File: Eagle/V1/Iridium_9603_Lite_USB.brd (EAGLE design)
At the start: 34.7 x 44.2 mm, 26 parts, among them J1 SS4-10-3.50-X-D, J2 uFL, U1 SPX3819M5-L-3-3, U2 LTC3225EDDB-TRMPBFDFN300X200-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, U3 CY7C65213

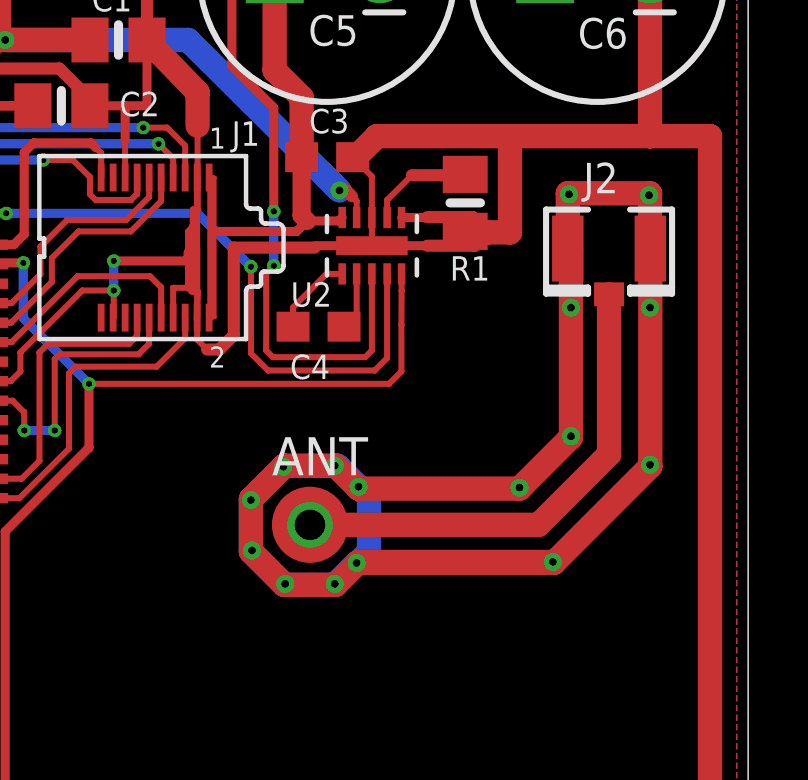
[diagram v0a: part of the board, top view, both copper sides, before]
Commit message: Updated ANT and GNDA to provide impedance of 50 Ohms
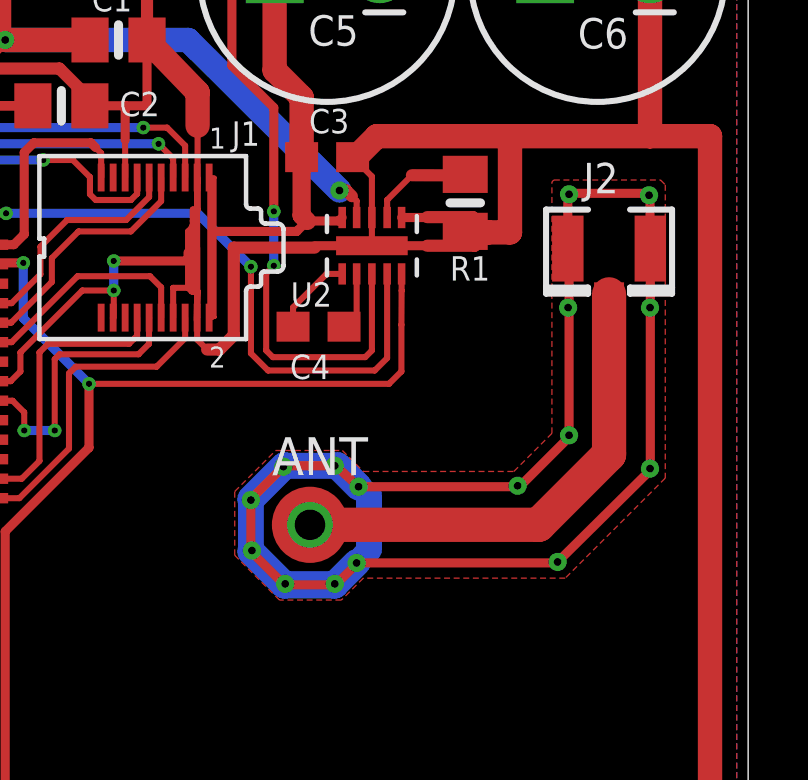
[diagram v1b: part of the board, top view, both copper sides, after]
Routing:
- net GNDA: track 69.2 -> 62.6 mm
- added copper zone on layer 1, net GNDA
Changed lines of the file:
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@@
 <wire x1="20.22475" y1="30.00375" x2="20.22475" y2="29.94025" width="0.127" layer="1"/>
 <wire x1="20.22475" y1="29.94025" x2="17.526" y2="29.94025" width="0.4064" layer="1"/>
-<polygon width="0.4064" layer="1" spacing="0.8128" pour="hatch" isolate="0.6096">
+<polygon width="0.4064" layer="1" spacing="0.8128" pour="hatch" isolate="0.6096" rank="2">
 <vertex x="0.381" y="0.381"/>
 <vertex x="0.381" y="43.815"/>
@@
 <contactref element="ANT" pad="TP"/>
 <contactref element="J2" pad="3"/>
-<wire x1="30.0355" y1="28.3835" x2="30.0355" y2="23.0505" width="0.8128" layer="1"/>
-<wire x1="30.0355" y1="23.0505" x2="27.686" y2="20.701" width="0.8128" layer="1"/>
-<wire x1="27.686" y1="20.701" x2="20.066" y2="20.701" width="0.8128" layer="1"/>
+<wire x1="30.0355" y1="28.3835" x2="30.0355" y2="23.0505" width="1.143" layer="1"/>
+<wire x1="30.0355" y1="23.0505" x2="27.686" y2="20.701" width="1.143" layer="1"/>
+<wire x1="27.686" y1="20.701" x2="20.066" y2="20.701" width="1.143" layer="1"/>
 <via x="20.066" y="20.701" extent="1-16" drill="1.016" diameter="1.397"/>
 </signal>
@@
 <contactref element="J2" pad="2"/>
 <contactref element="J2" pad="1"/>
-<wire x1="28.6605" y1="29.9085" x2="28.7655" y2="29.9085" width="0.8128" layer="1"/>
-<wire x1="28.7655" y1="29.9085" x2="28.7655" y2="23.622" width="0.8128" layer="1"/>
-<wire x1="28.7655" y1="23.622" x2="27.051" y2="21.9075" width="0.8128" layer="1"/>
-<wire x1="27.051" y1="21.9075" x2="21.68525" y2="21.9075" width="0.8128" layer="1"/>
-<wire x1="21.68525" y1="21.9075" x2="20.92325" y2="22.6695" width="0.8128" layer="1"/>
-<wire x1="20.92325" y1="22.6695" x2="19.20875" y2="22.6695" width="0.8128" layer="1"/>
-<wire x1="19.20875" y1="22.6695" x2="18.0975" y2="21.55825" width="0.8128" layer="1"/>
-<wire x1="18.0975" y1="21.55825" x2="18.0975" y2="19.812" width="0.8128" layer="1"/>
-<wire x1="18.0975" y1="19.812" x2="19.20875" y2="18.70075" width="0.8128" layer="1"/>
-<wire x1="19.20875" y1="18.70075" x2="20.92325" y2="18.70075" width="0.8128" layer="1"/>
-<wire x1="20.92325" y1="18.70075" x2="21.6535" y2="19.431" width="0.8128" layer="1"/>
-<wire x1="21.6535" y1="19.431" x2="28.194" y2="19.431" width="0.8128" layer="1"/>
-<wire x1="28.194" y1="19.431" x2="31.4105" y2="22.6475" width="0.8128" layer="1"/>
-<wire x1="31.4105" y1="22.6475" x2="31.4105" y2="29.9085" width="0.8128" layer="1"/>
-<wire x1="28.6605" y1="29.9085" x2="28.6605" y2="31.75" width="0.8128" layer="1"/>
-<wire x1="28.6605" y1="31.75" x2="31.40075" y2="31.75" width="0.8128" layer="1"/>
-<wire x1="31.40075" y1="31.75" x2="31.40075" y2="29.845" width="0.8128" layer="1"/>
+<wire x1="28.6605" y1="29.9085" x2="28.702" y2="29.9085" width="0.8128" layer="1"/>
+<wire x1="28.702" y1="29.9085" x2="28.702" y2="23.622" width="0.3048" layer="1"/>
+<wire x1="28.702" y1="23.622" x2="27.051" y2="21.971" width="0.3048" layer="1"/>
+<wire x1="27.051" y1="21.971" x2="21.68525" y2="21.971" width="0.3048" layer="1"/>
+<wire x1="21.68525" y1="21.971" x2="20.92325" y2="22.6695" width="0.3048" layer="1"/>
+<wire x1="20.92325" y1="22.6695" x2="19.20875" y2="22.6695" width="0.3048" layer="1"/>
+<wire x1="19.20875" y1="22.6695" x2="18.0975" y2="21.55825" width="0.3048" layer="1"/>
+<wire x1="18.0975" y1="21.55825" x2="18.0975" y2="19.812" width="0.3048" layer="1"/>
+<wire x1="18.0975" y1="19.812" x2="19.20875" y2="18.70075" width="0.3048" layer="1"/>
+<wire x1="19.20875" y1="18.70075" x2="20.92325" y2="18.70075" width="0.3048" layer="1"/>
+<wire x1="20.92325" y1="18.70075" x2="21.6535" y2="19.431" width="0.3048" layer="1"/>
+<wire x1="21.6535" y1="19.431" x2="28.321" y2="19.431" width="0.3048" layer="1"/>
+<wire x1="31.4105" y1="22.5205" x2="31.4105" y2="29.9085" width="0.3048" layer="1"/>
+<wire x1="28.6605" y1="29.9085" x2="28.6605" y2="31.75" width="0.3048" layer="1"/>
+<wire x1="28.6605" y1="31.75" x2="31.40075" y2="31.75" width="0.3048" layer="1"/>
+<wire x1="31.40075" y1="31.75" x2="31.40075" y2="29.845" width="0.3048" layer="1"/>
 <via x="28.702" y="31.71825" extent="1-16" drill="0.254" diameter="0.6096"/>
 <via x="31.369" y="31.6865" extent="1-16" drill="0.254" diameter="0.6096"/>
-<via x="28.7655" y="23.65375" extent="1-16" drill="0.254" diameter="0.6096"/>
-<via x="31.40075" y="22.70125" extent="1-16" drill="0.254" diameter="0.6096"/>
-<via x="27.051" y="21.93925" extent="1-16" drill="0.254" diameter="0.6096"/>
-<via x="28.16225" y="19.46275" extent="1-16" drill="0.254" diameter="0.6096"/>
+<via x="28.702" y="23.6855" extent="1-16" drill="0.254" diameter="0.6096"/>
+<via x="31.40075" y="22.57425" extent="1-16" drill="0.254" diameter="0.6096"/>
+<via x="26.9875" y="22.00275" extent="1-16" drill="0.254" diameter="0.6096"/>
+<via x="28.321" y="19.46275" extent="1-16" drill="0.254" diameter="0.6096"/>
 <via x="21.62175" y="19.431" extent="1-16" drill="0.254" diameter="0.6096"/>
 <via x="20.8915" y="18.7325" extent="1-16" drill="0.254" diameter="0.6096"/>
@@
 <vertex x="34.29" y="0.381"/>
 </polygon>
-<wire x1="21.68525" y1="21.971" x2="20.98675" y2="22.6695" width="0.8128" layer="16"/>
-<wire x1="20.98675" y1="22.6695" x2="19.20875" y2="22.6695" width="0.8128" layer="16"/>
-<wire x1="19.20875" y1="22.6695" x2="18.0975" y2="21.55825" width="0.8128" layer="16"/>
-<wire x1="18.0975" y1="21.55825" x2="18.0975" y2="19.812" width="0.8128" layer="16"/>
-<wire x1="18.0975" y1="19.812" x2="19.20875" y2="18.70075" width="0.8128" layer="16"/>
-<wire x1="19.20875" y1="18.70075" x2="20.8915" y2="18.70075" width="0.8128" layer="16"/>
-<wire x1="20.8915" y1="18.70075" x2="21.62175" y2="19.431" width="0.8128" layer="16"/>
-<wire x1="21.68525" y1="21.971" x2="22.0345" y2="21.62175" width="0.8128" layer="16"/>
-<wire x1="22.0345" y1="21.62175" x2="22.0345" y2="19.812" width="0.8128" layer="16"/>
-<wire x1="22.0345" y1="19.812" x2="21.6535" y2="19.431" width="0.8128" layer="16"/>
-<via x="28.7655" y="27.94" extent="1-16" drill="0.254" diameter="0.6096"/>
+<wire x1="21.68525" y1="21.971" x2="20.98675" y2="22.6695" width="0.9144" layer="16"/>
+<wire x1="20.98675" y1="22.6695" x2="19.20875" y2="22.6695" width="0.8636" layer="16"/>
+<wire x1="19.20875" y1="22.6695" x2="18.0975" y2="21.55825" width="0.9144" layer="16"/>
+<wire x1="18.0975" y1="21.55825" x2="18.0975" y2="19.812" width="0.8636" layer="16"/>
+<wire x1="18.0975" y1="19.812" x2="19.20875" y2="18.70075" width="0.9144" layer="16"/>
+<wire x1="19.20875" y1="18.70075" x2="20.8915" y2="18.70075" width="0.9144" layer="16"/>
+<wire x1="20.8915" y1="18.70075" x2="21.62175" y2="19.431" width="0.9144" layer="16"/>
+<wire x1="21.68525" y1="21.971" x2="22.0345" y2="21.68525" width="0.8128" layer="16"/>
+<wire x1="22.0345" y1="21.68525" x2="22.0345" y2="19.8755" width="0.8636" layer="16"/>
+<wire x1="22.0345" y1="19.8755" x2="21.6535" y2="19.431" width="0.8128" layer="16"/>
+<via x="28.67025" y="27.94" extent="1-16" drill="0.254" diameter="0.6096"/>
 <via x="31.40075" y="27.94" extent="1-16" drill="0.254" diameter="0.6096"/>
-<wire x1="21.6535" y1="19.431" x2="21.68525" y2="19.46275" width="0.8128" layer="1"/>
-<wire x1="21.68525" y1="19.46275" x2="28.16225" y2="19.46275" width="0.8128" layer="1"/>
+<wire x1="21.6535" y1="19.431" x2="21.68525" y2="19.46275" width="0.3048" layer="1"/>
+<wire x1="28.321" y1="19.46275" x2="31.4105" y2="22.5205" width="0.3048" layer="1"/>
+<polygon width="0.3048" layer="1" isolate="0.16001875" thermals="no">
+<vertex x="26.8605" y="22.479"/>
+<vertex x="28.1305" y="23.749"/>
+<vertex x="28.1305" y="32.131"/>
+<vertex x="28.194" y="32.1945"/>
+<vertex x="31.75" y="32.1945"/>
+<vertex x="31.90875" y="32.03575"/>
+<vertex x="31.90875" y="22.25675"/>
+<vertex x="28.575" y="18.923"/>
+<vertex x="21.844" y="18.923"/>
+<vertex x="21.11375" y="18.19275"/>
+<vertex x="19.05" y="18.19275"/>
+<vertex x="17.55775" y="19.685"/>
+<vertex x="17.55775" y="21.81225"/>
+<vertex x="18.923" y="23.1775"/>
+<vertex x="21.1455" y="23.1775"/>
+<vertex x="21.844" y="22.479"/>
+</polygon>
 </signal>
 <signal name="NC1">
